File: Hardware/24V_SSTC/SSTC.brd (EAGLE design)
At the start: 100 x 90 mm, 40 parts, among them IC1 NE555, J5 PIN1-2, Q1 IRF512, Q2 IRF512, Q3 BUZ11BH, Q4 BUZ11BH, T1 BD242C, T2 BD242C

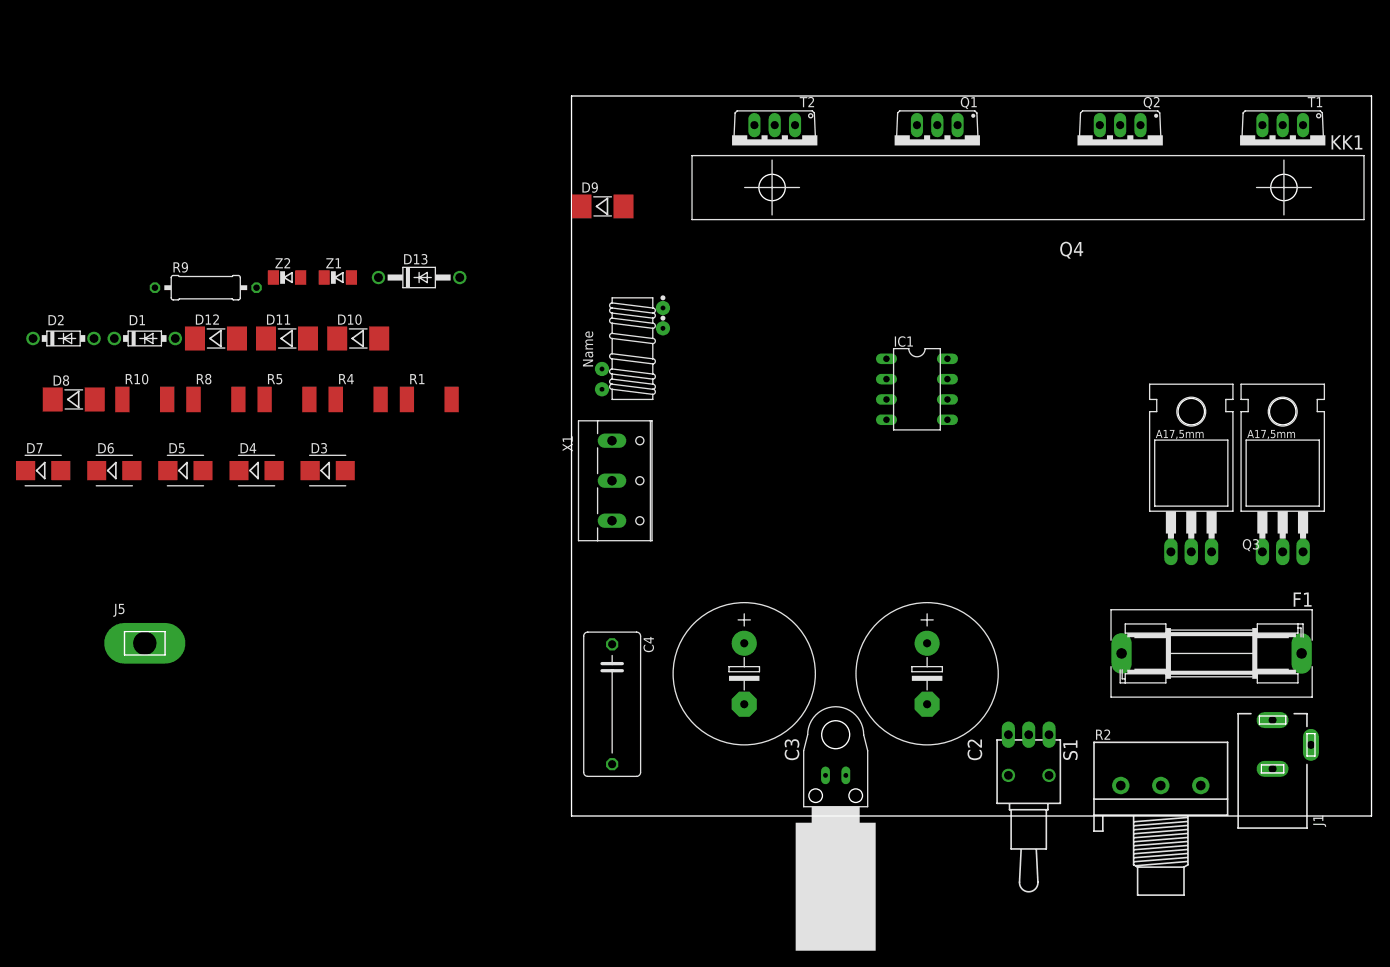
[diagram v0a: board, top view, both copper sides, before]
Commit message: Fertigstellung der SSTC Kleinere Bugfixes im UI
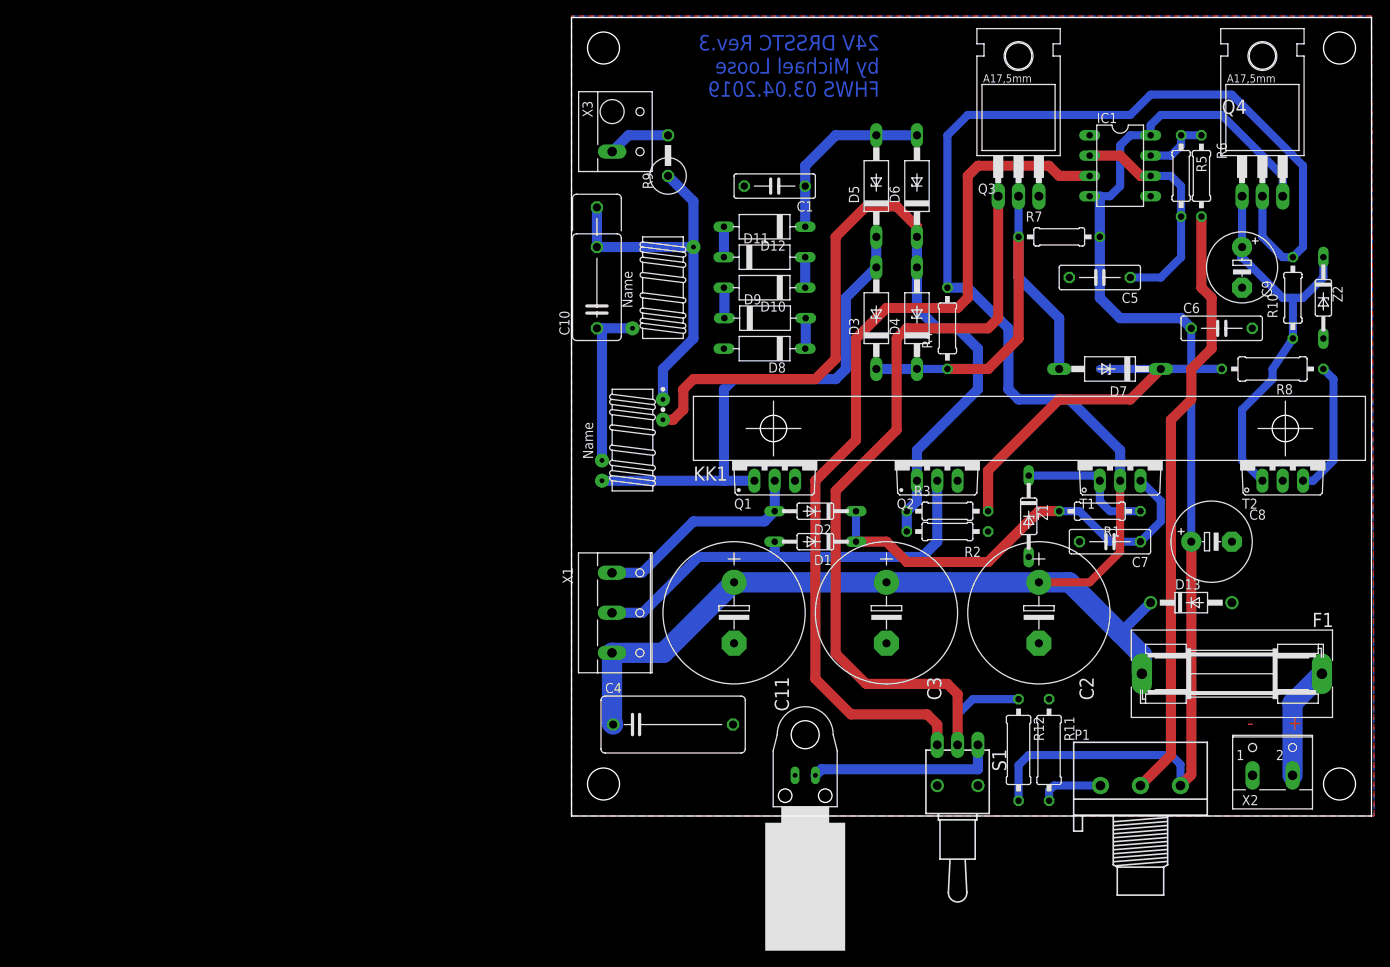
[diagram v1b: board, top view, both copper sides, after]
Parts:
- removed J1: (no value), con-jack:DCJ0303
- removed J5: PIN1-2, con-faston:62221
- added C1, C5, C6, C7: 100n, rcl:C075-032X103
- added C10: (no value), rcl:C102_152-062X184
- added C11: (no value), rcl:E7,5-18
- added C8: 1m, rcl:E5-10,5
- added C9: 22µ, rcl:E5-8,5
- added P1: (no value), pot:3RP/1610N
- added R11: 168k, rcl:0309/12
- added R12: 22k, rcl:0309/12
- added R3: 80k, rcl:0207/10
- added R6: 168k, rcl:0207/10
- added R7: 22k, rcl:0207/10
- added U$3: T50_INDUCTOR, toroid:T50_INDUCTOR
- added X2: (no value), con-wago-500:W237-102
- added X3: (no value), con-wago-500:W237-112
- D1, D2: device diode:DO41-7.6 -> diode:DO35-10
- D10, D11, D12, D8, D9: device diode:MELF-MLL41 -> diode:D-10
- D3, D4, D5, D6, D7: device diode:SMB -> diode:F126Z12
- R1, R10, R4, R5: device rcl:R2512 -> rcl:0207/10
- R2: value (none) -> 38k; device pot:3RP/1610N -> rcl:0207/10
- R8: device rcl:R2512 -> rcl:0309/12
- R9: device rcl:0309/12 -> rcl:P0613V
- Z1, Z2: device diode:SOD80C -> diode:DO35Z10
- moved R10 144.1 mm to (90.2, 64.8), turned to 90 degrees
- moved D7 134.0 mm to (67.3, 55.9), turned to 180 degrees
- moved R8 132.1 mm to (87.6, 55.9), turned to 180 degrees
- moved Z2 129.6 mm to (94.0, 64.8), turned to 270 degrees
- moved R5 115.2 mm to (76.2, 80.0), turned to 270 degrees
- moved D6 106.4 mm to (43.2, 78.7), turned to 90 degrees
- moved D13 104.7 mm to (77.5, 26.7)
- moved D2 96.4 mm to (30.5, 38.1), turned to 180 degrees
- moved D5 93.4 mm to (38.1, 78.7), turned to 90 degrees
- moved Z1 91.4 mm to (57.1, 37.5), turned to 270 degrees
- moved D1 87.6 mm to (30.5, 34.3), turned to 180 degrees
- moved D8 86.6 mm to (24.1, 58.4), turned to 180 degrees
- moved R1 85.0 mm to (66.0, 38.1), turned to 180 degrees
- moved D4 84.7 mm to (43.2, 62.2), turned to 90 degrees
- moved T2 74.7 mm to (88.9, 44.5), turned to 0 degrees
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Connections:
- removed net VCC+: IC1.8
- new net N$16: C9.+, Q4.G, R10.1, T2.1, Z2.C
- new net N$17: R8.1, T2.3
- new net N$18: IC1.7, R5.1, R6.1
- new net N$19: C5.1, IC1.2, IC1.6, R5.2
- new net N$20: P1.2, R6.2
- new net N$21: P1.1, R11.2
- new net N$22: Q3.G, R12.1, S1.2
- new net N$23: IC1.3, S1.3
- new net N$24: S1.1, U$2.A
- new net VCC/2: C6.1, C8.+, D7.C, IC1.4, IC1.8, P1.3, Q4.S, R12.2, R3.2, R7.2, R8.2
- net GND: now also C1.2, C10.1, C11.-, C5.2, C6.2, C7.2, C8.-, C9.-, Q3.S, R11.1, R2.1, T2.2, U$2.K, U$3.CA, X2.1, Z2.A; no longer J1.1
- net N$10: now also D7.A, Q3.D, R7.1
- net N$11: now also C7.1, D2.C
- net N$13: now also C10.2, U$3.CB
- net N$14: now also X3.1; no longer J5.1
- net N$15: now also X2.2; no longer J1.2, J1.3
- net N$5: now also C1.1
- net N$6: now also R2.2, R3.1, U$1.C1B; no longer U$1.C1A
- net N$7: now also U$1.C1A; no longer U$1.C1B
- net VCC: now also C11.+, Q4.D, R10.2
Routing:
- net VCC: track 0.00 -> 240.5 mm
- net VCC/2: track 0.00 -> 204.3 mm
- net N$23: track 0.00 -> 112.4 mm
- net N$22: track 0.00 -> 107.4 mm
- net N$6: track 0.00 -> 100.7 mm
- net N$20: track 0.00 -> 75.3 mm
- net N$7: track 0.00 -> 64.9 mm
- net N$10: track 0.00 -> 55.8 mm
- net N$11: track 0.00 -> 54.4 mm
- net N$8: track 0.00 -> 53.9 mm
- net N$16: track 0.00 -> 51.0 mm
- net N$13: track 0.00 -> 48.0 mm
- net N$19: track 0.00 -> 29.3 mm
- net N$9: track 0.00 -> 27.3 mm
- net N$24: track 0.00 -> 23.7 mm
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- added copper zone on layer 1, net GND
- added copper zone on layer 16, net GND
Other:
- board size 100 x 90 mm -> 100 x 99.8 mm
- board text added: "+"
- board text added: "-"
- board text added: "24V DRSSTC Rev.3 by Michael Loose FHWS 03.04.2019"
